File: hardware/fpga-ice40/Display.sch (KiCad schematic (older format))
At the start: 8 parts, among them Q1 2N7002H

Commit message: Add title and licensing info to documents
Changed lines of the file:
@@
 encoding utf-8
 Sheet 12 12
-Title ""
-Date ""
-Rev ""
-Comp ""
-Comment1 ""
+Title "Ferk-Cart iCE40 Devboard"
+Date "2020-06-29"
+Rev "r0.1"
+Comp "Designed by: Nelson Gauthier"
+Comment1 "Licensed under CERN OHL v.1.2"
 Comment2 ""
 Comment3 ""
@@
 	6200 5150 6400 5150
 Wire Wire Line
-	6400 5150 6500 5150
-Wire Wire Line
-	6500 5150 6600 5150
-Connection ~ 6500 5150
-Wire Wire Line
-	6500 5250 6500 5150
+	6200 5250 6200 5150
 $Comp
 L ng_power:GND #PWR?
 U 1 1 5F920840
-P 6500 5250
+P 6200 5250
 AR Path="/5F920840" Ref="#PWR?"  Part="1"
 AR Path="/5F90C399/5F920840" Ref="#PWR0127"  Part="1"
-F 0 "#PWR0127" H 6500 5000 50  0001 C CNN
-F 1 "GND" H 6503 5124 50  0000 C CNN
-F 2 "" H 6400 4900 50  0001 C CNN
-F 3 "" H 6500 5250 50  0001 C CNN
-	1    6500 5250
+F 0 "#PWR0127" H 6200 5000 50  0001 C CNN
+F 1 "GND" H 6203 5124 50  0000 C CNN
+F 2 "" H 6100 4900 50  0001 C CNN
+F 3 "" H 6200 5250 50  0001 C CNN
+	1    6200 5250
 	1    0    0    -1
 $EndComp
@@
 	1    0    0    -1
 $EndComp
+Connection ~ 6200 5150
+Wire Wire Line
+	6400 5150 6600 5150
 $EndSCHEMATC

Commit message: Reannotate schematic symbols
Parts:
- renumbered R5 to R10, R7 to R11
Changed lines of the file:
@@
 P 6200 5250
 AR Path="/5F920840" Ref="#PWR?"  Part="1"
-AR Path="/5F90C399/5F920840" Ref="#PWR0127"  Part="1"
-F 0 "#PWR0127" H 6200 5000 50  0001 C CNN
+AR Path="/5F90C399/5F920840" Ref="#PWR034"  Part="1"
+F 0 "#PWR034" H 6200 5000 50  0001 C CNN
 F 1 "GND" H 6203 5124 50  0000 C CNN
 F 2 "" H 6100 4900 50  0001 C CNN
@@
 P 6200 4300
 AR Path="/5F920849" Ref="R?"  Part="4"
-AR Path="/5F90C399/5F920849" Ref="R7"  Part="4"
-F 0 "R7" V 6250 4450 50  0000 L CNN
+AR Path="/5F90C399/5F920849" Ref="R11"  Part="4"
+F 0 "R11" V 6250 4450 50  0000 L CNN
 F 1 "330R" V 6250 4150 50  0000 R CNN
 F 2 "Resistor_SMD:R_Array_Convex_4x0603" V 6130 4300 50  0001 C CNN
@@
 P 6400 4300
 AR Path="/5F920858" Ref="R?"  Part="3"
-AR Path="/5F90C399/5F920858" Ref="R7"  Part="3"
-F 0 "R7" V 6450 4450 50  0000 L CNN
+AR Path="/5F90C399/5F920858" Ref="R11"  Part="3"
+F 0 "R11" V 6450 4450 50  0000 L CNN
 F 1 "330R" V 6450 4150 50  0000 R CNN
 F 2 "Resistor_SMD:R_Array_Convex_4x0603" V 6330 4300 50  0001 C CNN
@@
 P 6600 4300
 AR Path="/5F920867" Ref="R?"  Part="2"
-AR Path="/5F90C399/5F920867" Ref="R7"  Part="2"
-F 0 "R7" V 6650 4450 50  0000 L CNN
+AR Path="/5F90C399/5F920867" Ref="R11"  Part="2"
+F 0 "R11" V 6650 4450 50  0000 L CNN
 F 1 "330R" V 6650 4150 50  0000 R CNN
 F 2 "Resistor_SMD:R_Array_Convex_4x0603" V 6530 4300 50  0001 C CNN
@@
 P 6800 4300
 AR Path="/5F920876" Ref="R?"  Part="1"
-AR Path="/5F90C399/5F920876" Ref="R7"  Part="1"
-F 0 "R7" V 6850 4450 50  0000 L CNN
+AR Path="/5F90C399/5F920876" Ref="R11"  Part="1"
+F 0 "R11" V 6850 4450 50  0000 L CNN
 F 1 "330R" V 6850 4150 50  0000 R CNN
 F 2 "Resistor_SMD:R_Array_Convex_4x0603" V 6730 4300 50  0001 C CNN
@@
 P 4700 3950
 AR Path="/5F920889" Ref="R?"  Part="1"
-AR Path="/5F90C399/5F920889" Ref="R5"  Part="1"
-F 0 "R5" H 4770 3996 50  0000 L CNN
+AR Path="/5F90C399/5F920889" Ref="R10"  Part="1"
+F 0 "R10" H 4770 3996 50  0000 L CNN
 F 1 "470R" H 4770 3905 50  0000 L CNN
 F 2 "Resistor_SMD:R_0603_1608Metric" V 4630 3950 50  0001 C CNN
@@
 P 4700 5100
 AR Path="/5F920896" Ref="#PWR?"  Part="1"
-AR Path="/5F90C399/5F920896" Ref="#PWR0128"  Part="1"
-F 0 "#PWR0128" H 4700 4850 50  0001 C CNN
+AR Path="/5F90C399/5F920896" Ref="#PWR033"  Part="1"
+F 0 "#PWR033" H 4700 4850 50  0001 C CNN
 F 1 "GND" H 4703 4974 50  0000 C CNN
 F 2 "" H 4600 4750 50  0001 C CNN

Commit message: Component selection by MPN and routing cleanup
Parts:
- Q1: value 2N7002H -> 2N7002H-7; MPN (none) -> 2N7002H-7
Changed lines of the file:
@@
 AR Path="/5F90C399/5F92089C" Ref="Q1"  Part="1"
 F 0 "Q1" H 4805 4846 50  0000 L CNN
-F 1 "2N7002H" H 4805 4755 50  0000 L CNN
+F 1 "2N7002H-7" H 4805 4755 50  0000 L CNN
 F 2 "Package_TO_SOT_SMD:SOT-23" H 4800 4725 50  0001 L CIN
 F 3 "http://www.diodes.com/assets/Datasheets/2N7002H.pdf" H 4600 4800 50  0001 L CNN
+F 4 "2N7002H-7" H 4600 4800 50  0001 C CNN "MPN"
 	1    4600 4800
 	1    0    0    -1

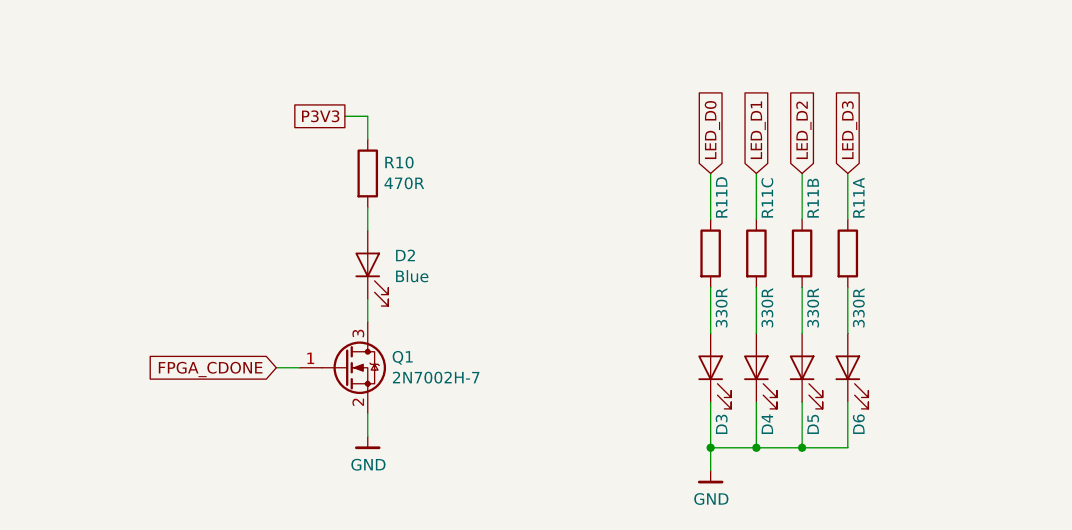
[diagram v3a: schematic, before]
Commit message: Complete component selection by MPN
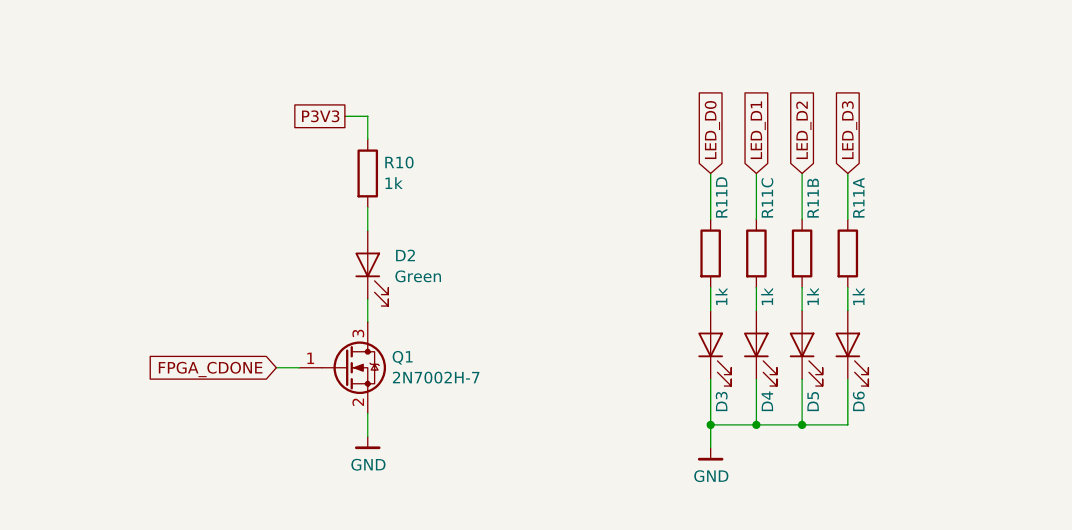
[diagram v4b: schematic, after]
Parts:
- D2, D3, D4, D5, D6: value Blue -> Green; MPN (none) -> LTST-C190GKT
- R10: value 470R -> 1k; MPN (none) -> RC0603JR-071KL
- R11: value 330R -> 1k; MPN (none) -> YC164-JR-071KL
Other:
- moved on the sheet: D3, D4, D5, D6
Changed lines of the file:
@@
 $EndDescr
 Wire Wire Line
-	6400 4950 6400 5150
-Wire Wire Line
-	6600 5150 6800 5150
-Connection ~ 6600 5150
-Wire Wire Line
-	6600 4950 6600 5150
-Wire Wire Line
-	6800 5150 6800 4950
-Wire Wire Line
-	6200 4950 6200 5150
-Connection ~ 6400 5150
-Wire Wire Line
-	6200 5150 6400 5150
-Wire Wire Line
-	6200 5250 6200 5150
+	6400 4850 6400 5050
+Wire Wire Line
+	6600 5050 6800 5050
+Connection ~ 6600 5050
+Wire Wire Line
+	6600 4850 6600 5050
+Wire Wire Line
+	6800 5050 6800 4850
+Wire Wire Line
+	6200 4850 6200 5050
+Connection ~ 6400 5050
+Wire Wire Line
+	6200 5050 6400 5050
+Wire Wire Line
+	6200 5150 6200 5050
 $Comp
 L ng_power:GND #PWR?
 U 1 1 5F920840
-P 6200 5250
+P 6200 5150
 AR Path="/5F920840" Ref="#PWR?"  Part="1"
 AR Path="/5F90C399/5F920840" Ref="#PWR034"  Part="1"
-F 0 "#PWR034" H 6200 5000 50  0001 C CNN
-F 1 "GND" H 6203 5124 50  0000 C CNN
-F 2 "" H 6100 4900 50  0001 C CNN
-F 3 "" H 6200 5250 50  0001 C CNN
-	1    6200 5250
+F 0 "#PWR034" H 6200 4900 50  0001 C CNN
+F 1 "GND" H 6203 5024 50  0000 C CNN
+F 2 "" H 6100 4800 50  0001 C CNN
+F 3 "" H 6200 5150 50  0001 C CNN
+	1    6200 5150
 	1    0    0    -1
 $EndComp
@@
 Wire Wire Line
 	6800 4150 6800 3950
-Wire Wire Line
-	6800 4650 6800 4450
 $Comp
 L Device:R_Pack04_Split R?
@@
 AR Path="/5F90C399/5F920849" Ref="R11"  Part="4"
 F 0 "R11" V 6250 4450 50  0000 L CNN
-F 1 "330R" V 6250 4150 50  0000 R CNN
+F 1 "1k" V 6250 4150 50  0000 R CNN
 F 2 "Resistor_SMD:R_Array_Convex_4x0603" V 6130 4300 50  0001 C CNN
 F 3 "~" H 6200 4300 50  0001 C CNN
+F 4 "YC164-JR-071KL" H 6200 4300 50  0001 C CNN "MPN"
 	4    6200 4300
 	1    0    0    -1
@@
 L Device:LED D?
 U 1 1 5F92084F
-P 6800 4800
+P 6800 4700
 AR Path="/5F92084F" Ref="D?"  Part="1"
 AR Path="/5F90C399/5F92084F" Ref="D6"  Part="1"
-F 0 "D6" H 6600 4750 50  0000 R CNN
-F 1 "Blue" H 6550 4750 50  0001 R CNN
-F 2 "LED_SMD:LED_0603_1608Metric" H 6800 4800 50  0001 C CNN
-F 3 "~" H 6800 4800 50  0001 C CNN
-	1    6800 4800
+F 0 "D6" H 6600 4650 50  0000 R CNN
+F 1 "Green" H 6550 4650 50  0001 R CNN
+F 2 "LED_SMD:LED_0603_1608Metric" H 6800 4700 50  0001 C CNN
+F 3 "~" H 6800 4700 50  0001 C CNN
+F 4 "LTST-C190GKT" H 6800 4700 50  0001 C CNN "MPN"
+	1    6800 4700
 	0    -1   -1   0
 $EndComp
@@
 Wire Wire Line
 	6600 4150 6600 3950
-Wire Wire Line
-	6600 4650 6600 4450
 $Comp
 L Device:R_Pack04_Split R?
@@
 AR Path="/5F90C399/5F920858" Ref="R11"  Part="3"
 F 0 "R11" V 6450 4450 50  0000 L CNN
-F 1 "330R" V 6450 4150 50  0000 R CNN
+F 1 "1k" V 6450 4150 50  0000 R CNN
 F 2 "Resistor_SMD:R_Array_Convex_4x0603" V 6330 4300 50  0001 C CNN
 F 3 "~" H 6400 4300 50  0001 C CNN
+F 4 "YC164-JR-071KL" H 6400 4300 50  0001 C CNN "MPN"
 	3    6400 4300
 	1    0    0    -1
@@
 L Device:LED D?
 U 1 1 5F92085E
-P 6600 4800
+P 6600 4700
 AR Path="/5F92085E" Ref="D?"  Part="1"
 AR Path="/5F90C399/5F92085E" Ref="D5"  Part="1"
-F 0 "D5" H 6400 4750 50  0000 R CNN
-F 1 "Blue" H 6350 4750 50  0001 R CNN
-F 2 "LED_SMD:LED_0603_1608Metric" H 6600 4800 50  0001 C CNN
-F 3 "~" H 6600 4800 50  0001 C CNN
-	1    6600 4800
+F 0 "D5" H 6400 4650 50  0000 R CNN
+F 1 "Green" H 6350 4650 50  0001 R CNN
+F 2 "LED_SMD:LED_0603_1608Metric" H 6600 4700 50  0001 C CNN
+F 3 "~" H 6600 4700 50  0001 C CNN
+F 4 "LTST-C190GKT" H 6600 4700 50  0001 C CNN "MPN"
+	1    6600 4700
 	0    -1   -1   0
 $EndComp
@@
 Wire Wire Line
 	6400 4150 6400 3950
-Wire Wire Line
-	6400 4650 6400 4450
 $Comp
 L Device:R_Pack04_Split R?
@@
 AR Path="/5F90C399/5F920867" Ref="R11"  Part="2"
 F 0 "R11" V 6650 4450 50  0000 L CNN
-F 1 "330R" V 6650 4150 50  0000 R CNN
+F 1 "1k" V 6650 4150 50  0000 R CNN
 F 2 "Resistor_SMD:R_Array_Convex_4x0603" V 6530 4300 50  0001 C CNN
 F 3 "~" H 6600 4300 50  0001 C CNN
+F 4 "YC164-JR-071KL" H 6600 4300 50  0001 C CNN "MPN"
 	2    6600 4300
 	1    0    0    -1
@@
 L Device:LED D?
 U 1 1 5F92086D
-P 6400 4800
+P 6400 4700
 AR Path="/5F92086D" Ref="D?"  Part="1"
 AR Path="/5F90C399/5F92086D" Ref="D4"  Part="1"
-F 0 "D4" H 6200 4750 50  0000 R CNN
-F 1 "Blue" H 6150 4750 50  0001 R CNN
-F 2 "LED_SMD:LED_0603_1608Metric" H 6400 4800 50  0001 C CNN
-F 3 "~" H 6400 4800 50  0001 C CNN
-	1    6400 4800
+F 0 "D4" H 6200 4650 50  0000 R CNN
+F 1 "Green" H 6150 4650 50  0001 R CNN
+F 2 "LED_SMD:LED_0603_1608Metric" H 6400 4700 50  0001 C CNN
+F 3 "~" H 6400 4700 50  0001 C CNN
+F 4 "LTST-C190GKT" H 6400 4700 50  0001 C CNN "MPN"
+	1    6400 4700
 	0    -1   -1   0
 $EndComp
@@
 Wire Wire Line
 	6200 4150 6200 3950
-Wire Wire Line
-	6200 4650 6200 4450
 $Comp
 L Device:R_Pack04_Split R?
@@
 AR Path="/5F90C399/5F920876" Ref="R11"  Part="1"
 F 0 "R11" V 6850 4450 50  0000 L CNN
-F 1 "330R" V 6850 4150 50  0000 R CNN
+F 1 "1k" V 6850 4150 50  0000 R CNN
 F 2 "Resistor_SMD:R_Array_Convex_4x0603" V 6730 4300 50  0001 C CNN
 F 3 "~" H 6800 4300 50  0001 C CNN
+F 4 "YC164-JR-071KL" H 6800 4300 50  0001 C CNN "MPN"
 	1    6800 4300
 	1    0    0    -1
@@
 L Device:LED D?
 U 1 1 5F92087C
-P 6200 4800
+P 6200 4700
 AR Path="/5F92087C" Ref="D?"  Part="1"
 AR Path="/5F90C399/5F92087C" Ref="D3"  Part="1"
-F 0 "D3" H 6000 4750 50  0000 R CNN
-F 1 "Blue" H 5950 4750 50  0001 R CNN
-F 2 "LED_SMD:LED_0603_1608Metric" H 6200 4800 50  0001 C CNN
-F 3 "~" H 6200 4800 50  0001 C CNN
-	1    6200 4800
+F 0 "D3" H 6000 4650 50  0000 R CNN
+F 1 "Green" H 5950 4650 50  0001 R CNN
+F 2 "LED_SMD:LED_0603_1608Metric" H 6200 4700 50  0001 C CNN
+F 3 "~" H 6200 4700 50  0001 C CNN
+F 4 "LTST-C190GKT" H 6200 4700 50  0001 C CNN "MPN"
+	1    6200 4700
 	0    -1   -1   0
 $EndComp
@@
 AR Path="/5F90C399/5F920889" Ref="R10"  Part="1"
 F 0 "R10" H 4770 3996 50  0000 L CNN
-F 1 "470R" H 4770 3905 50  0000 L CNN
+F 1 "1k" H 4770 3905 50  0000 L CNN
 F 2 "Resistor_SMD:R_0603_1608Metric" V 4630 3950 50  0001 C CNN
 F 3 "~" H 4700 3950 50  0001 C CNN
+F 4 "RC0603JR-071KL" H 4700 3950 50  0001 C CNN "MPN"
 	1    4700 3950
 	1    0    0    -1
@@
 AR Path="/5F90C399/5F92088F" Ref="D2"  Part="1"
 F 0 "D2" V 4739 4233 50  0000 R CNN
-F 1 "Blue" V 4648 4233 50  0000 R CNN
+F 1 "Green" V 4648 4233 50  0000 R CNN
 F 2 "LED_SMD:LED_0603_1608Metric" H 4700 4350 50  0001 C CNN
 F 3 "~" H 4700 4350 50  0001 C CNN
+F 4 "LTST-C190GKT" H 4700 4350 50  0001 C CNN "MPN"
 	1    4700 4350
 	0    -1   -1   0
@@
 	1    0    0    -1
 $EndComp
-Connection ~ 6200 5150
-Wire Wire Line
-	6400 5150 6600 5150
+Connection ~ 6200 5050
+Wire Wire Line
+	6400 5050 6600 5050
+Wire Wire Line
+	6200 4450 6200 4550
+Wire Wire Line
+	6400 4550 6400 4450
+Wire Wire Line
+	6600 4550 6600 4450
+Wire Wire Line
+	6800 4550 6800 4450
 $EndSCHEMATC

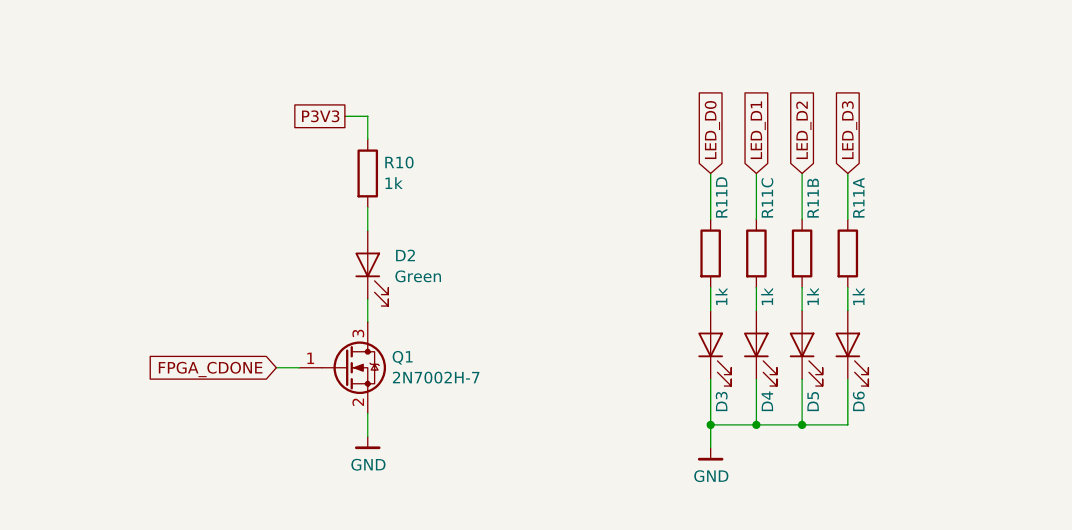
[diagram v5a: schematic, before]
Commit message: Fix mechanical issue by moving USB connector to top of board
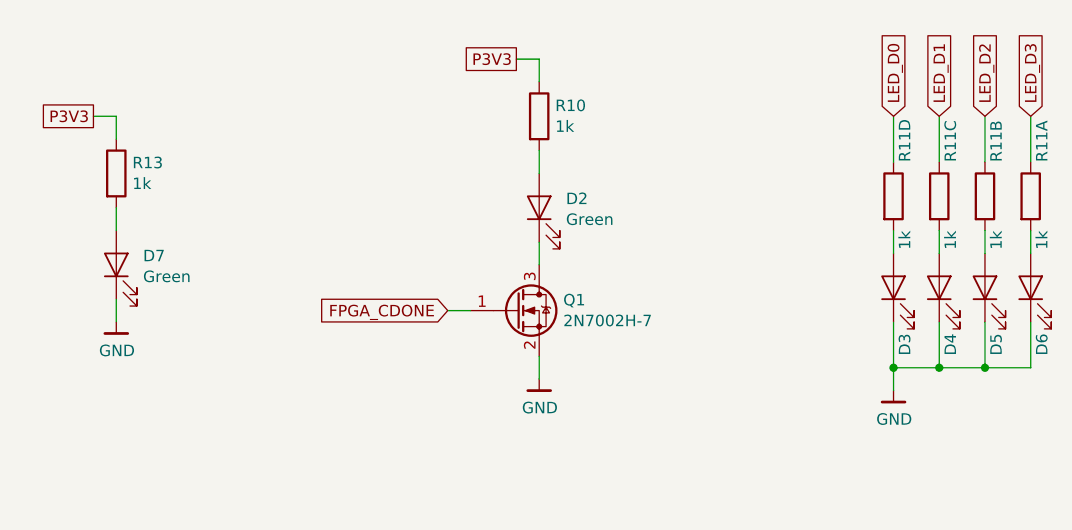
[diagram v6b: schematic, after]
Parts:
- added D7: Green, LED_SMD:LED_0603_1608Metric, symbol Device:LED
- added R13: 1k, Resistor_SMD:R_0603_1608Metric, symbol Device:R
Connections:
- net GND: now also D7.1 (K)
- net P3V3: now also R13.1
- new net: D7.2 (A), R13.2
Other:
- moved on the sheet: D2, D3, D4, D5, D6, Q1, R10, R11A, R11B, R11C, R11D
